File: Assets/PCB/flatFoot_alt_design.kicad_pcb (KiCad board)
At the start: 2 copper layers, 124.5 x 63.5 mm, 18 parts

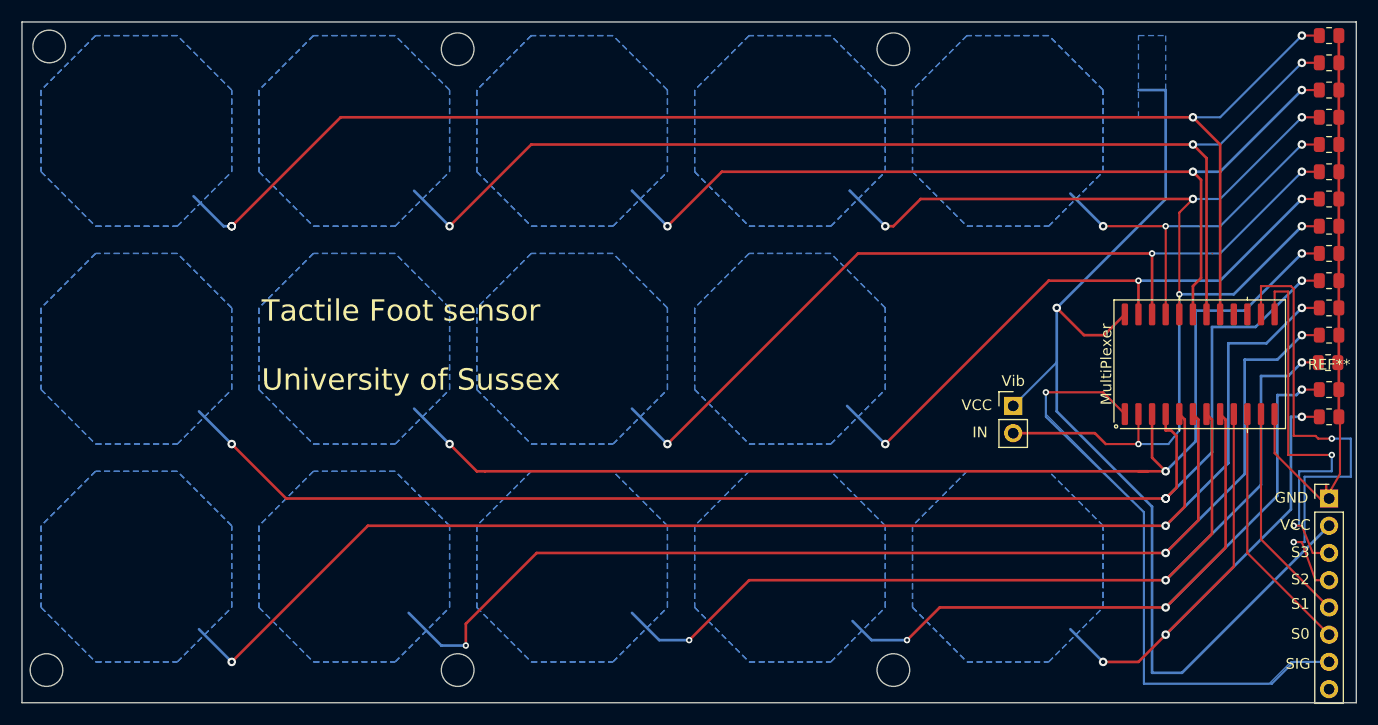
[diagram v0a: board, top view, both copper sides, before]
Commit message: updated PCBs for one layer
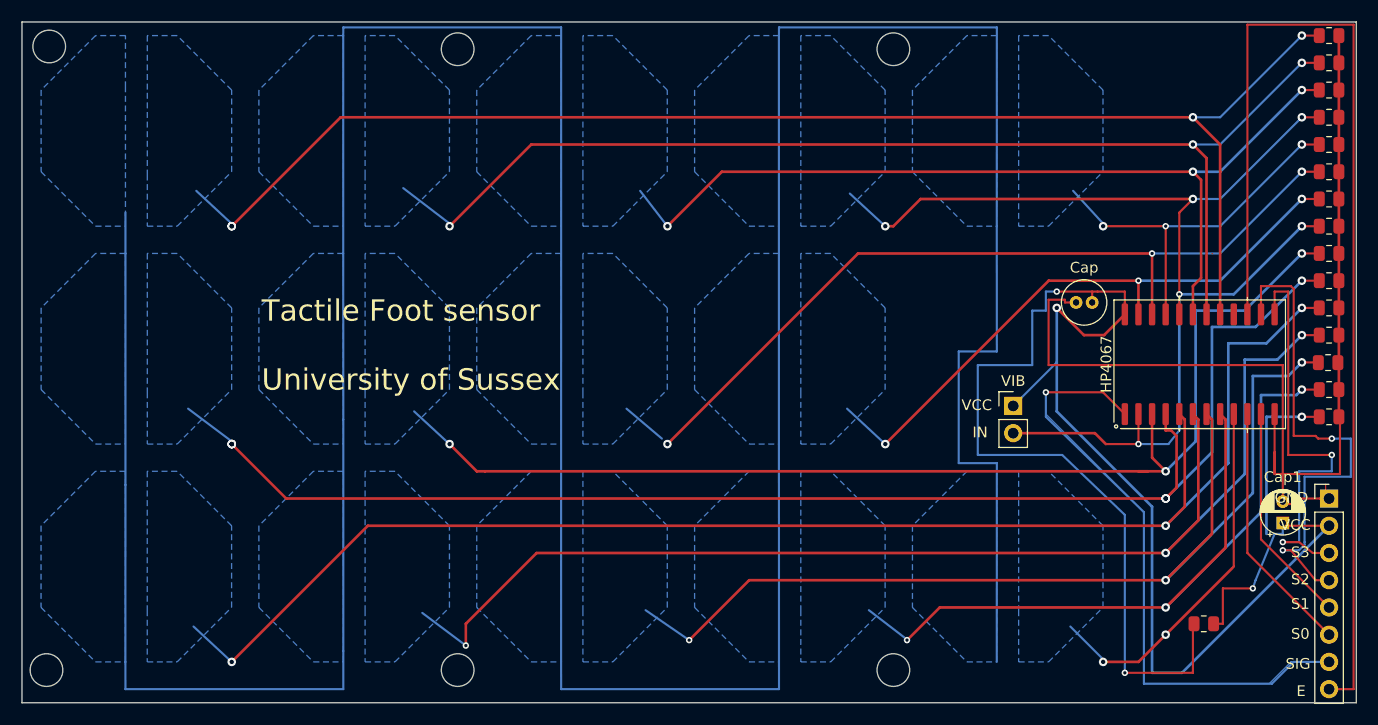
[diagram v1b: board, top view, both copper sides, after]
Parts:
- added Cap: C_Radial_D4.0mm_H5.0mm_P1.50mm, Capacitor_THT:C_Radial_D4.0mm_H5.0mm_P1.50mm, F.Cu at (199.9, 78.2)
- added Cap1: CP_Radial_D4.0mm_P2.00mm, Capacitor_THT:CP_Radial_D4.0mm_P2.00mm, F.Cu at (219.2, 98.8)
- added RP: R_0805_2012Metric, Resistor_SMD:R_0805_2012Metric, F.Cu at (211.8, 108.2)
- renumbered MultiPlexer to HP4067, Vib to VIB, REF** to gpio, REF** to j0, REF** to j1, REF** to j10, REF** to j11, REF** to j12, REF** to j13, REF** to j14, REF** to j2, REF** to j3, REF** to j4, REF** to j5, REF** to j6, REF** to j7, REF** to j8, REF** to j9
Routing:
- net (no net): track 1846.7 -> 1733.9 mm, vias 53 -> 58
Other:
- board text added: "E"

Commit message: fixed PCBs
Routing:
- net (no net): track 1733.9 -> 1778.4 mm, vias 58 -> 59
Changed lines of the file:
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@@
   (gr_line (start 204.47 77.216) (end 204.47 78.74)
     (stroke (width 0.2) (type default)) (layer "F.Cu"))
+  (gr_line (start 214.122 113.538) (end 192.532 113.538)
+    (stroke (width 0.2) (type default)) (layer "F.Cu"))
   (gr_line (start 219.202 84.074) (end 219.202 94.234)
     (stroke (width 0.2) (type default)) (layer "F.Cu"))
@@
   (gr_line (start 220.98 73.66) (end 222.504 73.66)
     (stroke (width 0.2) (type default)) (layer "F.Cu"))
+  (gr_line (start 192.532 113.538) (end 192.278 113.538)
+    (stroke (width 0.2) (type default)) (layer "F.Cu"))
   (gr_line (start 215.9 52.324) (end 225.806 52.324)
     (stroke (width 0.2) (type default)) (layer "F.Cu"))
@@
   (gr_line (start 197.104 86.614) (end 202.438 86.614)
     (stroke (width 0.2) (type default)) (layer "F.Cu"))
+  (gr_line (start 216.408 104.902) (end 216.408 111.252)
+    (stroke (width 0.2) (type default)) (layer "F.Cu"))
   (gr_line (start 216.408 104.902) (end 213.614 104.902)
     (stroke (width 0.2) (type default)) (layer "F.Cu"))
@@
   (gr_line (start 223.012 99.06) (end 219.71 99.06)
     (stroke (width 0.2) (type default)) (layer "F.Cu"))
+  (gr_line (start 216.408 111.252) (end 214.122 113.538)
+    (stroke (width 0.2) (type default)) (layer "F.Cu"))
   (gr_line (start 218.44 94.234) (end 218.44 92.202)
     (stroke (width 0.2) (type default)) (layer "F.Cu"))
@@
     (stroke (width 0.2) (type default)) (layer "B.Cu"))
   (gr_line (start 172.205 53.34) (end 172.212 52.578)
+    (stroke (width 0.2) (type default)) (layer "B.Cu"))
+  (gr_line (start 192.525 111.76) (end 192.278 113.538)
     (stroke (width 0.2) (type default)) (layer "B.Cu"))
   (gr_line (start 131.572 110.744) (end 131.572 89.154)
@@
   (segment (start 219.964 76.708) (end 217.17 76.708) (width 0.2) (layer "F.Cu") (net 0))
   (segment (start 208.28 106.68) (end 213.868 101.092) (width 0.25) (layer "F.Cu") (net 0))
+  (segment (start 192.278 113.538) (end 214.122 113.538) (width 0) (layer "F.Cu") (net 0))
   (segment (start 217.17 100.33) (end 217.17 88.646) (width 0) (layer "F.Cu") (net 0))
   (segment (start 214.63 102.87) (end 214.503 102.997) (width 0.2) (layer "F.Cu") (net 0))
@@
   (segment (start 197.365 76.2) (end 182.125 91.44) (width 0.25) (layer "F.Cu") (net 0))
   (segment (start 206.6125 104.14) (end 169.425 104.14) (width 0) (layer "F.Cu") (net 0))
+  (segment (start 216.408 105.326264) (end 216.620132 105.114132) (width 0) (layer "F.Cu") (net 0))
   (segment (start 209.55 79.346) (end 209.55 69.85) (width 0.2) (layer "F.Cu") (net 0))
   (segment (start 218.44 77.216) (end 219.71 77.216) (width 0.2) (layer "F.Cu") (net 0))
@@
   (segment (start 211.582 75.946) (end 210.82 76.708) (width 0.25) (layer "F.Cu") (net 0))
   (segment (start 210.058 97.282) (end 210.058 89.154) (width 0.25) (layer "F.Cu") (net 0))
+  (segment (start 216.408 111.252) (end 216.408 105.326264) (width 0) (layer "F.Cu") (net 0))
   (segment (start 223.52 109.22) (end 215.9 101.6) (width 0) (layer "F.Cu") (net 0))
   (segment (start 208.28 101.6) (end 149.606 101.6) (width 0.25) (layer "F.Cu") (net 0))
@@
   (segment (start 205.74 76.2) (end 205.74 79.346) (width 0.25) (layer "F.Cu") (net 0))
   (segment (start 210.82 60.96) (end 131.325 60.96) (width 0.25) (layer "F.Cu") (net 0))
+  (segment (start 214.122 113.538) (end 216.408 111.252) (width 0) (layer "F.Cu") (net 0))
   (segment (start 149.606 101.6) (end 143.002 108.204) (width 0.25) (layer "F.Cu") (net 0))
   (segment (start 210.82 60.96) (end 213.36 63.5) (width 0.25) (layer "F.Cu") (net 0))
@@
   (via (at 220.98 88.9) (size 0.8) (drill 0.4) (layers "F.Cu" "B.Cu") (net 0))
   (via (at 208.28 71.12) (size 0.6) (drill 0.3) (layers "F.Cu" "B.Cu") (net 0))
+  (via (at 192.278 113.538) (size 0.6) (drill 0.3) (layers "F.Cu" "B.Cu") (net 0))
   (via (at 219.202 100.584) (size 0.6) (drill 0.3) (layers "F.Cu" "B.Cu") (net 0))
   (via (at 220.98 71.12) (size 0.8) (drill 0.4) (layers "F.Cu" "B.Cu") (net 0))
@@
   (segment (start 218.694 83.566) (end 220.98 81.28) (width 0.25) (layer "B.Cu") (net 0))
   (segment (start 206.248 97.79) (end 206.248 113.792) (width 0) (layer "B.Cu") (net 0))
+  (segment (start 217.678 99.822) (end 208.28 109.22) (width 0.25) (layer "B.Cu") (net 0))
   (segment (start 216.408 85.09) (end 219.71 85.09) (width 0.25) (layer "B.Cu") (net 0))
   (segment (start 141.485 91.44) (end 141.478 91.44) (width 0.25) (layer "B.Cu") (net 0))
